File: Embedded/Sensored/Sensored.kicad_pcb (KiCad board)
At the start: 2 copper layers, 15 x 15 mm, 35 parts, among them J1 SDA, J10 SCL, J11 SDA, J12 SCL, J13 3V3, J14 GND, J15 3V3, J16 GND, J2 3V3, J3 GND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

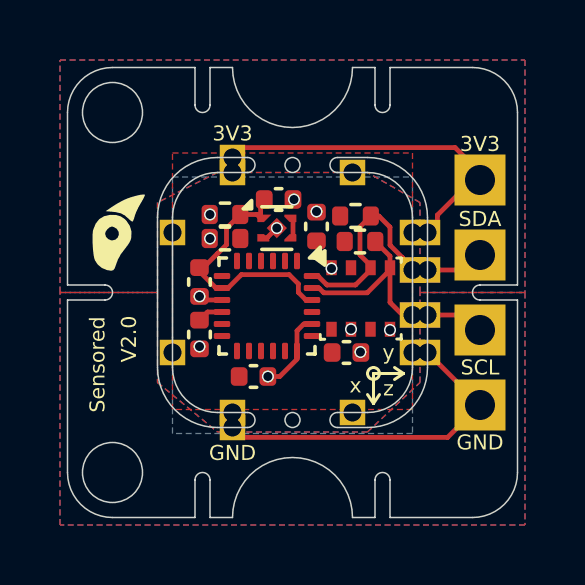
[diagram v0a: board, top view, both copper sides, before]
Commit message: Modified Board Edge to 0.8mm Tolerance
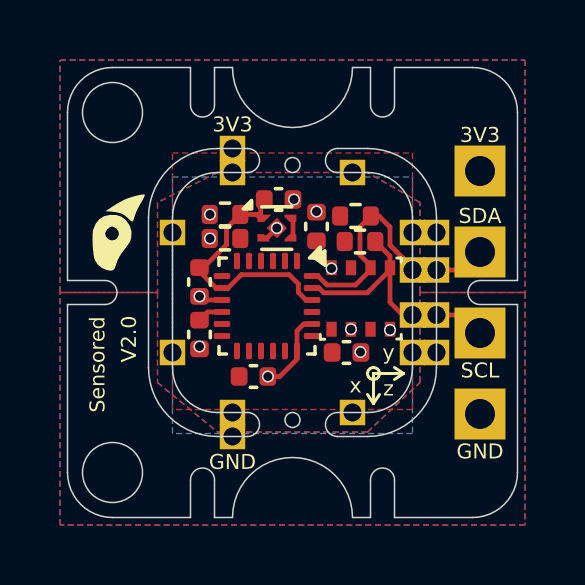
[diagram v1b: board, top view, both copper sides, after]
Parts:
- moved J11 0.30 mm to (79.8, 59.2)
- moved J12 0.30 mm to (79.8, 60.8)
- moved J13 0.30 mm to (79.8, 58.0)
- moved J14 0.30 mm to (79.8, 62.0)
- moved J15 0.30 mm to (73.0, 55.2)
- moved J16 0.30 mm to (73.0, 64.8)
- moved TP1 0.30 mm to (81.2, 56.0)
- moved TP4 0.30 mm to (81.2, 64.0)
- moved TP2 0.10 mm to (81.2, 58.6)
- moved TP3 0.10 mm to (81.2, 61.4)
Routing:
- net +3V3: track 12.0 -> 0.65 mm
- net GND: track 15.6 -> 4.86 mm
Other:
- outline, holes or cut-outs redrawn

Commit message: Modified the Pin Positions
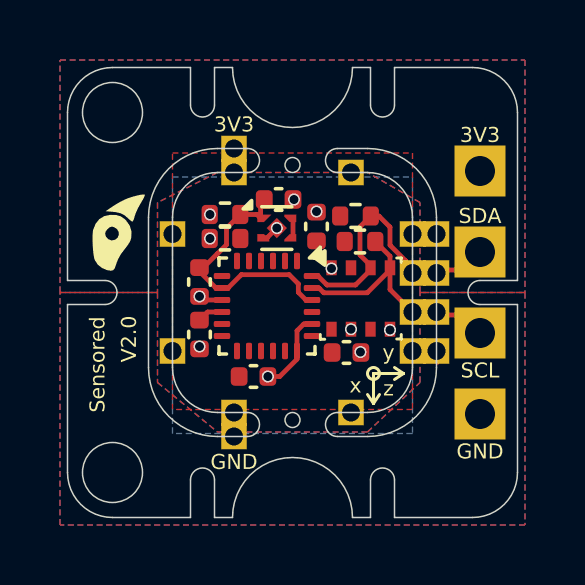
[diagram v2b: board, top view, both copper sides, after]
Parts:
- moved J1 0.10 mm to (79.0, 59.4)
- moved J10 0.10 mm to (79.0, 60.6)
- moved J11 0.10 mm to (79.8, 59.4)
- moved J12 0.10 mm to (79.8, 60.6)
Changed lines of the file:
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@@
 	(footprint "Custom Connectors:1mm Pads"
 		(layer "F.Cu")
-		(at 73 64.8)
+		(at 73.05 64.8)
 		(property "Reference" "J16"
 			(at 0 -1.2 0)
@@
 	(footprint "Custom Connectors:1mm Pads"
 		(layer "F.Cu")
-		(at 79.8 62)
+		(at 79.8 61.95)
 		(property "Reference" "J14"
 			(at 0 -1.2 0)
@@
 	(footprint "Custom Connectors:1mm Pads"
 		(layer "F.Cu")
-		(at 79.8 59.25)
+		(at 79.8 59.35)
 		(property "Reference" "J11"
 			(at 0 -1.2 0)
@@
 	(footprint "Custom Connectors:1mm Pads"
 		(layer "F.Cu")
-		(at 73 55.2)
+		(at 73.05 55.2)
 		(property "Reference" "J15"
 			(at 0 -1.2 0)
@@
 	(footprint "Custom Connectors:1mm Pads"
 		(layer "F.Cu")
-		(at 79.8 58)
+		(at 79.8 58.05)
 		(property "Reference" "J13"
 			(at 0 -1.2 0)
@@
 	(footprint "Custom Connectors:1mm Pads"
 		(layer "F.Cu")
-		(at 79.8 60.75)
+		(at 79.8 60.65)
 		(property "Reference" "J12"
 			(at 0 -1.2 0)
@@
 	(footprint "Custom Connectors:1mm Pads"
 		(layer "B.Cu")
-		(at 71 62)
+		(at 71 61.95)
 		(property "Reference" "J6"
 			(at 0 1.2 180)
@@
 	(footprint "Custom Connectors:1mm Pads"
 		(layer "B.Cu")
-		(at 79 62 180)
+		(at 79 61.95 180)
 		(property "Reference" "J3"
 			(at 0 1.2 0)
@@
 	(footprint "Custom Connectors:1mm Pads"
 		(layer "B.Cu")
-		(at 79 59.25 180)
+		(at 79 59.35 180)
 		(property "Reference" "J1"
 			(at 0 1.2 0)
@@
 	(footprint "Custom Connectors:1mm Pads"
 		(layer "B.Cu")
-		(at 73 56 -90)
+		(at 73.05 56 -90)
 		(property "Reference" "J4"
 			(at 0 1.2 90)
@@
 	(footprint "Custom Connectors:1mm Pads"
 		(layer "B.Cu")
-		(at 71 58)
+		(at 71 58.05)
 		(property "Reference" "J7"
 			(at 0 1.2 180)
@@
 	(footprint "Custom Connectors:1mm Pads"
 		(layer "B.Cu")
-		(at 79 60.75 180)
+		(at 79 60.65 180)
 		(property "Reference" "J10"
 			(at 0 1.2 0)
@@
 	(footprint "Custom Connectors:1mm Pads"
 		(layer "B.Cu")
-		(at 73 64 90)
+		(at 73.05 64 90)
 		(property "Reference" "J9"
 			(at 0 1.2 -90)
@@
 	(footprint "Custom Connectors:1mm Pads"
 		(layer "B.Cu")
-		(at 77 56 -90)
+		(at 76.95 56 -90)
 		(property "Reference" "J5"
 			(at 0 1.2 90)
@@
 	(footprint "Custom Connectors:1mm Pads"
 		(layer "B.Cu")
-		(at 79 58 180)
+		(at 79 58.05 180)
 		(property "Reference" "J2"
 			(at 0 1.2 0)
@@
 	(footprint "Custom Connectors:1mm Pads"
 		(layer "B.Cu")
-		(at 77 64 90)
+		(at 76.95 64 90)
 		(property "Reference" "J8"
 			(at 0 1.2 -90)
@@
 	)
 	(segment
+		(start 77.879999 57.45)
+		(end 78.25 57.820001)
+		(width 0.16)
+		(layer "F.Cu")
+		(net 9)
+	)
+	(segment
 		(start 75.65 59.45)
 		(end 75.851656 59.45)
@@
 	)
 	(segment
-		(start 78.25 57.820001)
-		(end 78.25 58.422305)
-		(width 0.16)
-		(layer "F.Cu")
-		(net 9)
-	)
-	(segment
 		(start 77.25 58.75)
 		(end 77.25 57.81)
@@
 	)
 	(segment
-		(start 78.67 58.842305)
-		(end 78.67 58.92)
+		(start 77.6 59.1)
+		(end 77.25 58.75)
 		(width 0.16)
 		(layer "F.Cu")
@@
 	)
 	(segment
-		(start 77.6 59.1)
-		(end 77.25 58.75)
+		(start 77.61 57.45)
+		(end 77.879999 57.45)
 		(width 0.16)
 		(layer "F.Cu")
@@
 	)
 	(segment
-		(start 77.879999 57.45)
-		(end 78.25 57.820001)
-		(width 0.16)
-		(layer "F.Cu")
-		(net 9)
-	)
-	(segment
 		(start 78.25 58.422305)
-		(end 78.67 58.842305)
+		(end 78.77 58.942305)
 		(width 0.16)
 		(layer "F.Cu")
@@
 	)
 	(segment
-		(start 77.61 57.45)
-		(end 77.879999 57.45)
+		(start 78.25 57.820001)
+		(end 78.25 58.422305)
 		(width 0.16)
 		(layer "F.Cu")
@@
 	)
 	(segment
+		(start 78.77 58.942305)
+		(end 78.77 59.35)
+		(width 0.16)
+		(layer "F.Cu")
+		(net 9)
+	)
+	(segment
 		(start 77.25 57.81)
 		(end 77.61 57.45)
@@
 	)
 	(segment
-		(start 78.25 59.175)
-		(end 78.25 60.33)
+		(start 78.21 59.134999)
+		(end 78.250001 59.175)
 		(width 0.16)
 		(layer "F.Cu")
@@
 	)
 	(segment
-		(start 78.21 59.134999)
-		(end 78.250001 59.175)
+		(start 77.76 58.300001)
+		(end 78.250001 58.790002)
 		(width 0.16)
 		(layer "F.Cu")
@@
 	)
 	(segment
-		(start 77.76 58.300001)
-		(end 78.250001 58.790002)
+		(start 78.25 59.175)
+		(end 78.25 59.9)
 		(width 0.16)
 		(layer "F.Cu")
@@
 	)
 	(segment
-		(start 78.250001 58.790002)
-		(end 78.250001 59.175)
+		(start 78.25 59.9)
+		(end 78.77 60.42)
 		(width 0.16)
 		(layer "F.Cu")
@@
 	)
 	(segment
-		(start 75.65 59.85)
-		(end 75.88396 59.85)
+		(start 78.250001 58.790002)
+		(end 78.250001 59.175)
 		(width 0.16)
 		(layer "F.Cu")
@@
 	)
 	(segment
-		(start 78.25 60.33)
-		(end 78.67 60.75)
+		(start 75.65 59.85)
+		(end 75.88396 59.85)
 		(width 0.16)
 		(layer "F.Cu")

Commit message: Modified Via Positions to prevent potential component floating
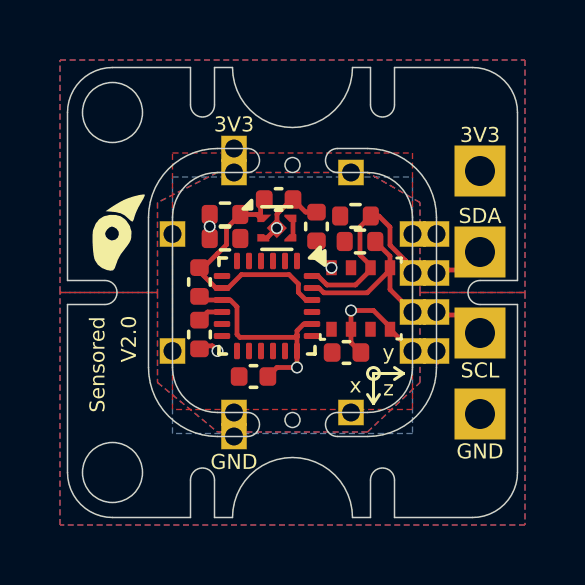
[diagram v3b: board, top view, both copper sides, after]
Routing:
- net GND: track 4.86 -> 16.1 mm, vias 12 -> 6
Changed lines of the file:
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@@
 	)
 	(segment
-		(start 74.18 62.800001)
-		(end 74.574999 62.800001)
+		(start 78.25 61.15)
+		(end 78.25 61.225)
+		(width 0.16)
+		(layer "F.Cu")
+		(net 1)
+	)
+	(segment
+		(start 74.4825 57.385869)
+		(end 74.4825 57.847501)
+		(width 0.16)
+		(layer "F.Cu")
+		(net 1)
+	)
+	(segment
+		(start 75.15 61.95)
+		(end 75.15 61.4)
+		(width 0.16)
+		(layer "F.Cu")
+		(net 1)
+	)
+	(segment
+		(start 75.15 62.5)
+		(end 74.480001 62.5)
+		(width 0.16)
+		(layer "F.Cu")
+		(net 1)
+	)
+	(segment
+		(start 73.245 61.495)
+		(end 75.15 61.495)
+		(width 0.16)
+		(layer "F.Cu")
+		(net 1)
+	)
+	(segment
+		(start 76.95 61.67)
+		(end 77.28 62)
 		(width 0.16)
 		(layer "F.Cu")
@@
 	)
 	(segment
-		(start 74.574999 62.800001)
-		(end 75.15 62.225)
-		(width 0.16)
-		(layer "F.Cu")
-		(net 1)
-	)
-	(segment
-		(start 72.24 58.200002)
-		(end 72.249998 58.200002)
-		(width 0.16)
-		(layer "F.Cu")
-		(net 1)
-	)
-	(segment
 		(start 75.0175 56.9)
 		(end 75.05 56.9)
@@
 	)
 	(segment
+		(start 75.15 61.495)
+		(end 75.15 61.4)
+		(width 0.16)
+		(layer "F.Cu")
+		(net 1)
+	)
+	(segment
+		(start 78.25 61.225)
+		(end 78.77 61.745)
+		(width 0.16)
+		(layer "F.Cu")
+		(net 1)
+	)
+	(segment
 		(start 79.83 62.33)
 		(end 79.83 61.86331)
@@
 	)
 	(segment
-		(start 75.15 62.225)
-		(end 75.15 61.95)
+		(start 72.925 60.25)
+		(end 73.15 60.475)
 		(width 0.16)
 		(layer "F.Cu")
@@
 	)
 	(segment
-		(start 75.15 61.95)
-		(end 75.15 61.275)
+		(start 75.8 57.320001)
+		(end 75.437501 57.320001)
+		(width 0.16)
+		(layer "F.Cu")
+		(net 1)
+	)
+	(segment
+		(start 73.15 60.475)
+		(end 73.15 61.4)
 		(width 0.16)
 		(layer "F.Cu")
@@
 	)
 	(segment
+		(start 76.95 60.6)
+		(end 76.95 61.67)
+		(width 0.16)
+		(layer "F.Cu")
+		(net 1)
+	)
+	(segment
 		(start 75.15 61.275)
 		(end 75.375 61.05)
@@
 	)
 	(segment
+		(start 75.15 61.4)
+		(end 75.15 61.275)
+		(width 0.16)
+		(layer "F.Cu")
+		(net 1)
+	)
+	(segment
+		(start 72.65 60.25)
+		(end 72.925 60.25)
+		(width 0.16)
+		(layer "F.Cu")
+		(net 1)
+	)
+	(segment
 		(start 75.375 61.05)
 		(end 75.65 61.05)
@@
 	)
 	(segment
-		(start 77.28 62)
-		(end 77.265 61.985)
-		(width 0.16)
-		(layer "F.Cu")
-		(net 1)
-	)
-	(segment
-		(start 72.249998 58.200002)
-		(end 72.25 58.2)
-		(width 0.16)
-		(layer "F.Cu")
-		(net 1)
-	)
-	(segment
-		(start 71.9 61.780001)
-		(end 71.9 61.8)
+		(start 74.4825 57.847501)
+		(end 74.4775 57.852501)
+		(width 0.16)
+		(layer "F.Cu")
+		(net 1)
+	)
+	(segment
+		(start 75.0175 56.9)
+		(end 74.968369 56.9)
+		(width 0.16)
+		(layer "F.Cu")
+		(net 1)
+	)
+	(segment
+		(start 77.7 60.6)
+		(end 78.25 61.15)
+		(width 0.16)
+		(layer "F.Cu")
+		(net 1)
+	)
+	(segment
+		(start 74.968369 56.9)
+		(end 74.4825 57.385869)
+		(width 0.16)
+		(layer "F.Cu")
+		(net 1)
+	)
+	(segment
+		(start 73.15 61.4)
+		(end 73.245 61.495)
+		(width 0.16)
+		(layer "F.Cu")
+		(net 1)
+	)
+	(segment
+		(start 75.437501 57.320001)
+		(end 75.0175 56.9)
 		(width 0.16)
 		(layer "F.Cu")
@@
 	)
 	(segment
-		(start 72.02 60.25)
-		(end 71.9 60.13)
-		(width 0.16)
-		(layer "F.Cu")
-		(net 1)
-	)
-	(segment
-		(start 76.3 59.175)
-		(end 76.3 59.2)
+		(start 75.15 62.5)
+		(end 75.15 61.95)
+		(width 0.16)
+		(layer "F.Cu")
+		(net 1)
+	)
+	(segment
+		(start 78.77 61.745)
+		(end 78.77 61.95)
+		(width 0.16)
+		(layer "F.Cu")
+		(net 1)
+	)
+	(segment
+		(start 72.330001 61.780001)
+		(end 72.5 61.95)
 		(width 0.16)
 		(layer "F.Cu")
@@
 		(net 1)
 	)
-	(via
-		(at 75.8 57.3)
-		(size 0.4)
-		(drill 0.3)
-		(layers "F.Cu" "B.Cu")
-		(net 1)
-	)
-	(via
-		(at 75.05 56.9)
-		(size 0.4)
-		(drill 0.3)
-		(layers "F.Cu" "B.Cu")
+	(segment
+		(start 71.9 61.780001)
+		(end 72.330001 61.780001)
+		(width 0.16)
+		(layer "F.Cu")
+		(net 1)
+	)
+	(segment
+		(start 76.95 60.6)
+		(end 77.7 60.6)
+		(width 0.16)
+		(layer "F.Cu")
+		(net 1)
+	)
+	(segment
+		(start 74.480001 62.5)
+		(end 74.18 62.800001)
+		(width 0.16)
+		(layer "F.Cu")
+		(net 1)
+	)
+	(segment
+		(start 72.24 57.4)
+		(end 72.24 58.200002)
+		(width 0.16)
+		(layer "F.Cu")
 		(net 1)
 	)
@@
 	)
 	(via
-		(at 76.3 59.2)
-		(size 0.4)
-		(drill 0.3)
-		(layers "F.Cu" "B.Cu")
-		(net 1)
-	)
-	(via
-		(at 74.18 62.800001)
-		(size 0.4)
-		(drill 0.3)
-		(layers "F.Cu" "B.Cu")
-		(net 1)
-	)
-	(via
-		(at 77.265 61.985)
-		(size 0.4)
-		(drill 0.3)
-		(layers "F.Cu" "B.Cu")
-		(net 1)
-	)
-	(via
-		(at 71.9 61.8)
-		(size 0.4)
-		(drill 0.3)
-		(layers "F.Cu" "B.Cu")
-		(net 1)
-	)
-	(via
-		(at 72.25 57.4)
-		(size 0.4)
-		(drill 0.3)
-		(layers "F.Cu" "B.Cu")
-		(net 1)
-	)
-	(via
-		(at 72.25 58.2)
-		(size 0.4)
-		(drill 0.3)
-		(layers "F.Cu" "B.Cu")
-		(net 1)
-	)
-	(via
-		(at 71.9 60.13)
-		(size 0.4)
-		(drill 0.3)
-		(layers "F.Cu" "B.Cu")
-		(net 1)
-	)
-	(via
-		(at 76.95 61.225)
-		(size 0.4)
-		(drill 0.3)
-		(layers "F.Cu" "B.Cu")
-		(net 1)
-	)
-	(via
-		(at 78.25 61.25)
-		(size 0.4)
-		(drill 0.3)
+		(at 76.3 59.175)
+		(size 0.4)
+		(drill 0.3)
+		(layers "F.Cu" "B.Cu")
+		(net 1)
+	)
+	(via
+		(at 75.15 62.5)
+		(size 0.4)
+		(drill 0.3)
+		(layers "F.Cu" "B.Cu")
+		(net 1)
+	)
+	(via
+		(at 72.5 61.95)
+		(size 0.4)
+		(drill 0.3)
+		(layers "F.Cu" "B.Cu")
+		(net 1)
+	)
+	(via
+		(at 72.24 57.8)
+		(size 0.4)
+		(drill 0.3)
+		(layers "F.Cu" "B.Cu")
+		(net 1)
+	)
+	(via
+		(at 76.95 60.6)
+		(size 0.4)
+		(drill 0.3)
